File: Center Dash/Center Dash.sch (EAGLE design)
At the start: 90 parts, among them J1 502585-0470, Q1 BSS138, Q2 BSS138, Q3 BSS138, Q4 BSS138, U1 ADG3304BRUZ-REEL7, U2 TPS54540DDARQ1

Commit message: Fixed?? amp seal connector
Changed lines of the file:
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@@
 <?xml version="1.0" encoding="utf-8"?>
 <!DOCTYPE eagle SYSTEM "eagle.dtd">
-<eagle version="8.6.1">
+<eagle version="8.7.0">
 <drawing>
 <settings>
@@
 <part name="GND20" library="supply1" deviceset="GND" device=""/>
 <part name="GND21" library="supply1" deviceset="GND" device=""/>
-<part name="U$1" library="FormE" deviceset="TE-776200-1" device=""/>
 <part name="GND22" library="supply1" deviceset="GND" device=""/>
 <part name="P+7" library="supply1" deviceset="+15V" device=""/>
@@
 <part name="GND37" library="supply1" deviceset="GND" device=""/>
 <part name="+3V6" library="supply1" library_urn="urn:adsk.eagle:library:371" deviceset="+3V3" device=""/>
+<part name="U$1" library="FormE" deviceset="TE-776200-1" device=""/>
 </parts>
 <sheets>
@@
 <instance part="GND20" gate="1" x="317.5" y="-124.46"/>
 <instance part="GND21" gate="1" x="281.94" y="-124.46"/>
-<instance part="U$1" gate="G$1" x="403.86" y="-243.84"/>
 <instance part="GND22" gate="1" x="254" y="-304.8"/>
 <instance part="P+7" gate="1" x="457.2" y="-203.2"/>
@@
 <instance part="GND37" gate="1" x="340.36" y="-271.78"/>
 <instance part="+3V6" gate="G$1" x="203.2" y="-175.26"/>
+<instance part="U$1" gate="G$1" x="401.32" y="-243.84"/>
 </instances>
 <busses>
@@
 </segment>
 <segment>
-<pinref part="U$1" gate="G$1" pin="P19"/>
 <wire x1="416.56" y1="-264.16" x2="480.06" y2="-264.16" width="0.1524" layer="91"/>
 <label x="474.98" y="-264.16" size="1.778" layer="95"/>
-</segment>
-<segment>
-<pinref part="U$1" gate="G$1" pin="P16"/>
+<pinref part="U$1" gate="G$1" pin="P19"/>
+</segment>
+<segment>
 <wire x1="416.56" y1="-256.54" x2="457.2" y2="-256.54" width="0.1524" layer="91"/>
 <label x="452.12" y="-256.54" size="1.778" layer="95"/>
+<pinref part="U$1" gate="G$1" pin="P16"/>
 </segment>
 <segment>
@@
 </segment>
 <segment>
-<pinref part="U$1" gate="G$1" pin="P5"/>
 <wire x1="416.56" y1="-223.52" x2="426.72" y2="-223.52" width="0.1524" layer="91"/>
 <label x="421.64" y="-223.52" size="1.778" layer="95"/>
+<pinref part="U$1" gate="G$1" pin="P5"/>
 </segment>
 <segment>
@@
 </segment>
 <segment>
-<pinref part="U$1" gate="G$1" pin="P1"/>
 <wire x1="416.56" y1="-213.36" x2="457.2" y2="-213.36" width="0.1524" layer="91"/>
 <wire x1="457.2" y1="-213.36" x2="457.2" y2="-205.74" width="0.1524" layer="91"/>
 <pinref part="P+7" gate="1" pin="+15V"/>
+<pinref part="U$1" gate="G$1" pin="P1"/>
 </segment>
 <segment>
@@
 </segment>
 <segment>
-<pinref part="U$1" gate="G$1" pin="P18"/>
 <wire x1="416.56" y1="-261.62" x2="480.06" y2="-261.62" width="0.1524" layer="91"/>
 <label x="474.98" y="-261.62" size="1.778" layer="95"/>
-</segment>
-<segment>
-<pinref part="U$1" gate="G$1" pin="P2"/>
+<pinref part="U$1" gate="G$1" pin="P18"/>
+</segment>
+<segment>
 <wire x1="416.56" y1="-215.9" x2="426.72" y2="-215.9" width="0.1524" layer="91"/>
 <label x="421.64" y="-215.9" size="1.778" layer="95"/>
+<pinref part="U$1" gate="G$1" pin="P2"/>
 </segment>
 <segment>
@@
 <net name="SERVO_PWM" class="0">
 <segment>
-<pinref part="U$1" gate="G$1" pin="P3"/>
 <wire x1="416.56" y1="-218.44" x2="426.72" y2="-218.44" width="0.1524" layer="91"/>
 <label x="421.64" y="-218.44" size="1.778" layer="95"/>
+<pinref part="U$1" gate="G$1" pin="P3"/>
 </segment>
 <segment>
@@
 </segment>
 <segment>
-<pinref part="U$1" gate="G$1" pin="P11"/>
 <wire x1="416.56" y1="-241.3" x2="439.42" y2="-241.3" width="0.1524" layer="91"/>
 <label x="424.18" y="-241.3" size="1.778" layer="95"/>
 <wire x1="439.42" y1="-241.3" x2="439.42" y2="-210.82" width="0.1524" layer="91"/>
 <pinref part="R3" gate="G$1" pin="2"/>
+<pinref part="U$1" gate="G$1" pin="P11"/>
 </segment>
 </net>
@@
 </segment>
 <segment>
-<pinref part="U$1" gate="G$1" pin="P12"/>
 <label x="424.18" y="-243.84" size="1.778" layer="95"/>
 <wire x1="416.56" y1="-243.84" x2="444.5" y2="-243.84" width="0.1524" layer="91"/>
 <wire x1="444.5" y1="-243.84" x2="444.5" y2="-210.82" width="0.1524" layer="91"/>
 <pinref part="R5" gate="G$1" pin="2"/>
+<pinref part="U$1" gate="G$1" pin="P12"/>
 </segment>
 </net>
 <net name="SPARE_1" class="0">
 <segment>
-<pinref part="U$1" gate="G$1" pin="P8"/>
 <wire x1="416.56" y1="-231.14" x2="429.26" y2="-231.14" width="0.1524" layer="91"/>
 <label x="424.18" y="-231.14" size="1.778" layer="95"/>
+<pinref part="U$1" gate="G$1" pin="P8"/>
 </segment>
 <segment>
@@
 </segment>
 <segment>
-<pinref part="U$1" gate="G$1" pin="P4"/>
 <wire x1="416.56" y1="-220.98" x2="426.72" y2="-220.98" width="0.1524" layer="91"/>
 <label x="421.64" y="-220.98" size="1.778" layer="95"/>
+<pinref part="U$1" gate="G$1" pin="P4"/>
 </segment>
 </net>
@@
 </segment>
 <segment>
-<pinref part="U$1" gate="G$1" pin="P20"/>
 <wire x1="416.56" y1="-266.7" x2="480.06" y2="-266.7" width="0.1524" layer="91"/>
 <label x="469.9" y="-266.7" size="1.778" layer="95"/>
+<pinref part="U$1" gate="G$1" pin="P20"/>
 </segment>
 </net>
@@
 </segment>
 <segment>
-<pinref part="U$1" gate="G$1" pin="P21"/>
 <wire x1="416.56" y1="-269.24" x2="480.06" y2="-269.24" width="0.1524" layer="91"/>
 <label x="469.9" y="-269.24" size="1.778" layer="95"/>
+<pinref part="U$1" gate="G$1" pin="P21"/>
 </segment>
 </net>
@@
 </segment>
 <segment>
-<pinref part="U$1" gate="G$1" pin="P22"/>
 <wire x1="416.56" y1="-271.78" x2="480.06" y2="-271.78" width="0.1524" layer="91"/>
 <label x="469.9" y="-271.78" size="1.778" layer="95"/>
+<pinref part="U$1" gate="G$1" pin="P22"/>
 </segment>
 </net>
@@
 </segment>
 <segment>
-<pinref part="U$1" gate="G$1" pin="P23"/>
 <wire x1="416.56" y1="-274.32" x2="480.06" y2="-274.32" width="0.1524" layer="91"/>
 <label x="469.9" y="-274.32" size="1.778" layer="95"/>
+<pinref part="U$1" gate="G$1" pin="P23"/>
 </segment>
 </net>
@@
 </segment>
 <segment>
-<pinref part="U$1" gate="G$1" pin="P6"/>
 <label x="449.58" y="-226.06" size="1.778" layer="95"/>
 <wire x1="416.56" y1="-226.06" x2="457.2" y2="-226.06" width="0.1524" layer="91"/>
+<pinref part="U$1" gate="G$1" pin="P6"/>
 </segment>
 </net>
@@
 </segment>
 <segment>
-<pinref part="U$1" gate="G$1" pin="P7"/>
 <label x="449.58" y="-228.6" size="1.778" layer="95"/>
 <wire x1="416.56" y1="-228.6" x2="457.2" y2="-228.6" width="0.1524" layer="91"/>
+<pinref part="U$1" gate="G$1" pin="P7"/>
 </segment>
 </net>
@@
 </segment>
 <segment>
-<pinref part="U$1" gate="G$1" pin="P10"/>
 <wire x1="416.56" y1="-238.76" x2="457.2" y2="-238.76" width="0.1524" layer="91"/>
 <label x="449.58" y="-238.76" size="1.778" layer="95"/>
+<pinref part="U$1" gate="G$1" pin="P10"/>
 </segment>
 </net>
@@
 </segment>
 <segment>
-<pinref part="U$1" gate="G$1" pin="P9"/>
 <wire x1="416.56" y1="-236.22" x2="457.2" y2="-236.22" width="0.1524" layer="91"/>
 <label x="449.58" y="-236.22" size="1.778" layer="95"/>
+<pinref part="U$1" gate="G$1" pin="P9"/>
 </segment>
 </net>
@@
 </segment>
 <segment>
-<pinref part="U$1" gate="G$1" pin="P17"/>
 <wire x1="416.56" y1="-259.08" x2="480.06" y2="-259.08" width="0.1524" layer="91"/>
 <label x="469.9" y="-259.08" size="1.778" layer="95"/>
+<pinref part="U$1" gate="G$1" pin="P17"/>
 </segment>
 </net>
@@
 </segment>
 <segment>
-<pinref part="U$1" gate="G$1" pin="P13"/>
 <wire x1="416.56" y1="-246.38" x2="480.06" y2="-246.38" width="0.1524" layer="91"/>
 <label x="469.9" y="-246.38" size="1.778" layer="95"/>
+<pinref part="U$1" gate="G$1" pin="P13"/>
 </segment>
 </net>
@@
 </segment>
 <segment>
-<pinref part="U$1" gate="G$1" pin="P14"/>
 <wire x1="416.56" y1="-248.92" x2="480.06" y2="-248.92" width="0.1524" layer="91"/>
 <label x="469.9" y="-248.92" size="1.778" layer="95"/>
+<pinref part="U$1" gate="G$1" pin="P14"/>
 </segment>
 </net>
@@
 </segment>
 <segment>
-<pinref part="U$1" gate="G$1" pin="P15"/>
 <wire x1="416.56" y1="-251.46" x2="480.06" y2="-251.46" width="0.1524" layer="91"/>
 <label x="469.9" y="-251.46" size="1.778" layer="95"/>
-</segment>
-</net>
+<pinref part="U$1" gate="G$1" pin="P15"/>
+</segment>
+</net>

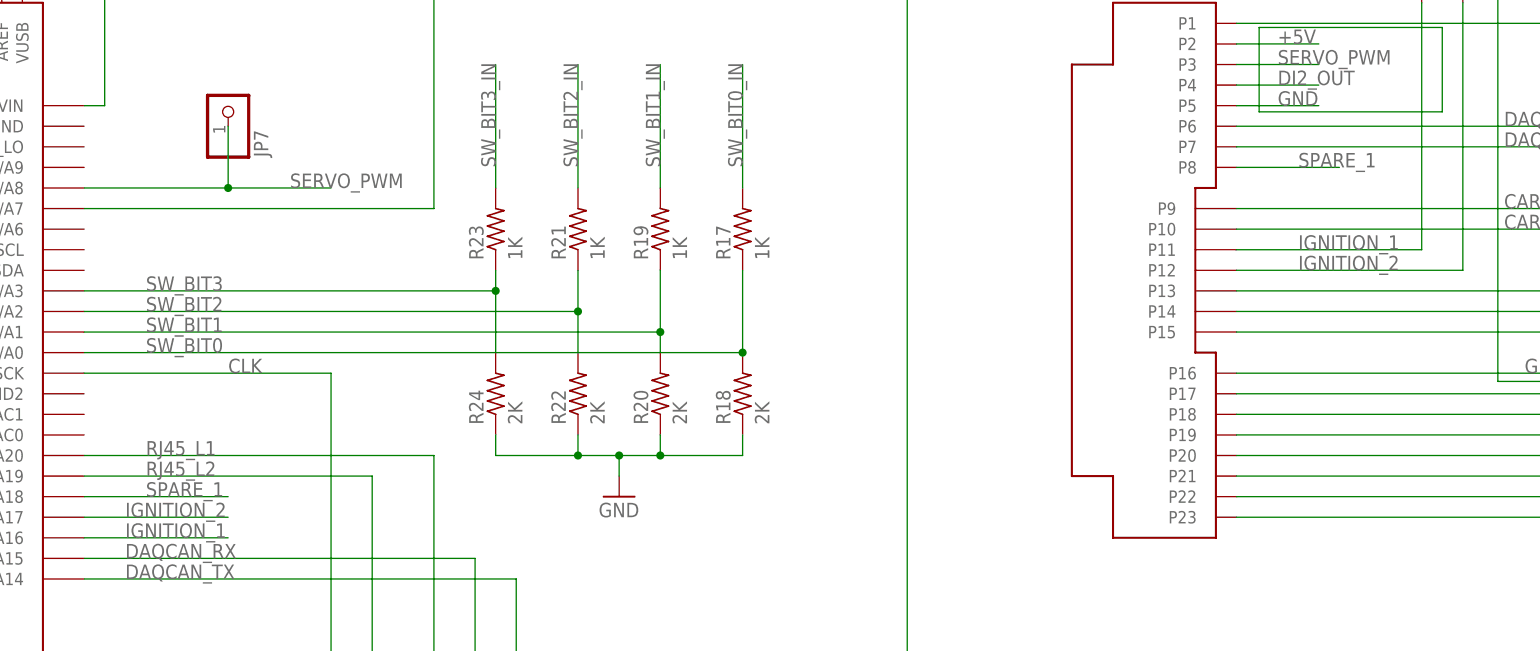
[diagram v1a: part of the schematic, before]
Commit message: Update schematic to remove last spare
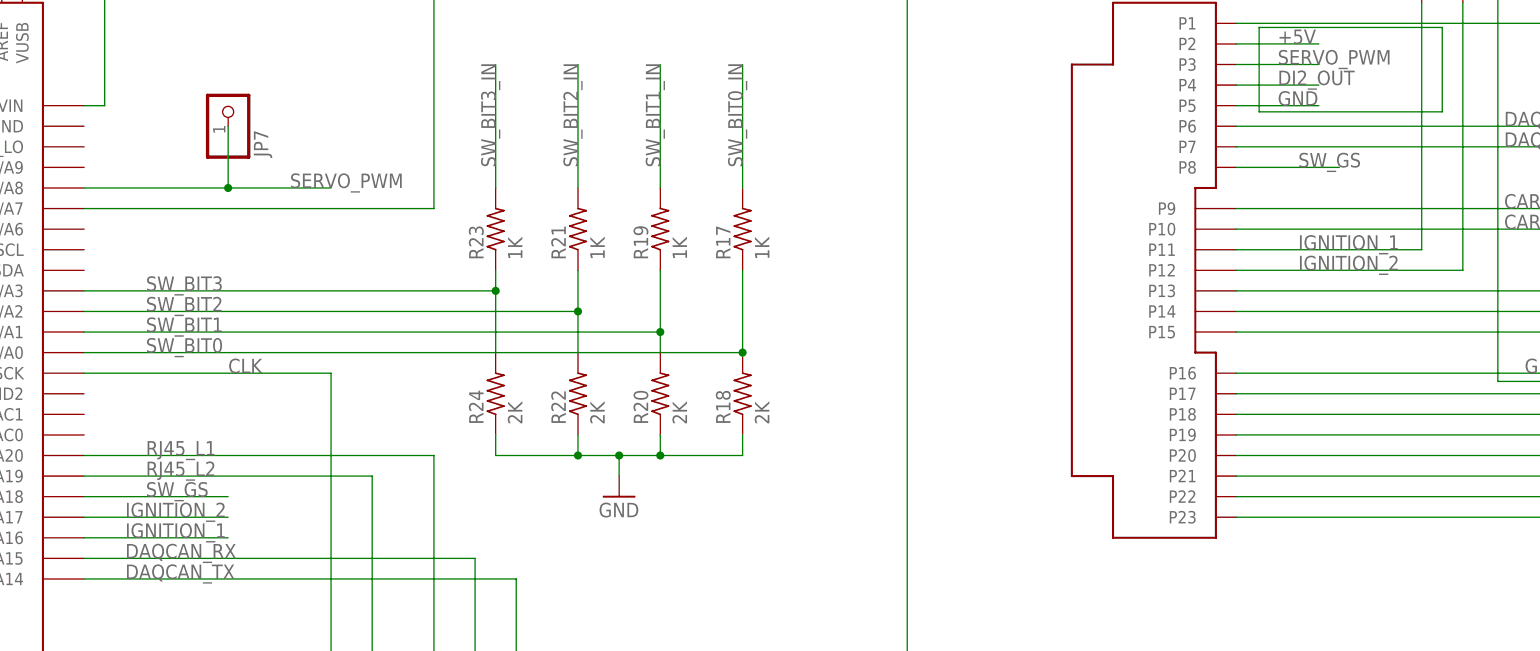
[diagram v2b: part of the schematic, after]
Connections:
- net SPARE_1 renamed SW_GS
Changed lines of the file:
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@@
-</segment>
-</net>
-<net name="SPARE_1" class="0">
-<segment>
-<wire x1="416.56" y1="-231.14" x2="429.26" y2="-231.14" width="0.1524" layer="91"/>
-<label x="424.18" y="-231.14" size="1.778" layer="95"/>
-<pinref part="U$1" gate="G$1" pin="P8"/>
-</segment>
-<segment>
-<pinref part="U$2" gate="G$1" pin="37/A18"/>
-<wire x1="274.32" y1="-271.78" x2="292.1" y2="-271.78" width="0.1524" layer="91"/>
-<label x="281.94" y="-271.78" size="1.778" layer="95"/>
 </segment>
 </net>
@@
 </segment>
 </net>
+<net name="SW_GS" class="0">
+<segment>
+<wire x1="416.56" y1="-231.14" x2="429.26" y2="-231.14" width="0.1524" layer="91"/>
+<label x="424.18" y="-231.14" size="1.778" layer="95"/>
+<pinref part="U$1" gate="G$1" pin="P8"/>
+</segment>
+<segment>
+<pinref part="U$2" gate="G$1" pin="37/A18"/>
+<wire x1="274.32" y1="-271.78" x2="292.1" y2="-271.78" width="0.1524" layer="91"/>
+<label x="281.94" y="-271.78" size="1.778" layer="95"/>
+</segment>
+</net>

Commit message: I dont remember
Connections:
- removed net N$1: LED2.GND
- net GND: now also LED2.GND
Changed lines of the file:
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@@
 <pinref part="LED6" gate="G$1" pin="GND"/>
 <wire x1="477.52" y1="-139.7" x2="477.52" y2="-144.78" width="0.1524" layer="91"/>
-<wire x1="477.52" y1="-144.78" x2="302.26" y2="-144.78" width="0.1524" layer="91"/>
+<wire x1="477.52" y1="-144.78" x2="444.5" y2="-144.78" width="0.1524" layer="91"/>
 <junction x="302.26" y="-144.78"/>
-</segment>
-<segment>
+<pinref part="LED2" gate="G$1" pin="GND"/>
+<wire x1="444.5" y1="-144.78" x2="408.94" y2="-144.78" width="0.1524" layer="91"/>
+<wire x1="408.94" y1="-144.78" x2="370.84" y2="-144.78" width="0.1524" layer="91"/>
+<wire x1="370.84" y1="-144.78" x2="335.28" y2="-144.78" width="0.1524" layer="91"/>
+<wire x1="335.28" y1="-144.78" x2="302.26" y2="-144.78" width="0.1524" layer="91"/>
+<wire x1="335.28" y1="-139.7" x2="335.28" y2="-144.78" width="0.1524" layer="91"/>
+<junction x="335.28" y="-144.78"/>
 <pinref part="LED3" gate="G$1" pin="GND"/>
 <wire x1="370.84" y1="-139.7" x2="370.84" y2="-144.78" width="0.1524" layer="91"/>
-</segment>
-<segment>
+<junction x="370.84" y="-144.78"/>
 <pinref part="LED4" gate="G$1" pin="GND"/>
 <wire x1="408.94" y1="-139.7" x2="408.94" y2="-144.78" width="0.1524" layer="91"/>
-</segment>
-<segment>
+<junction x="408.94" y="-144.78"/>
 <pinref part="LED5" gate="G$1" pin="GND"/>
 <wire x1="444.5" y1="-139.7" x2="444.5" y2="-144.78" width="0.1524" layer="91"/>
-</segment>
-<segment>
-<pinref part="LED8" gate="G$1" pin="GND"/>
-<wire x1="447.04" y1="-96.52" x2="447.04" y2="-101.6" width="0.1524" layer="91"/>
-</segment>
-<segment>
-<pinref part="LED9" gate="G$1" pin="GND"/>
-<wire x1="411.48" y1="-96.52" x2="411.48" y2="-101.6" width="0.1524" layer="91"/>
-</segment>
-<segment>
-<pinref part="LED10" gate="G$1" pin="GND"/>
-<wire x1="375.92" y1="-96.52" x2="375.92" y2="-101.6" width="0.1524" layer="91"/>
-</segment>
-<segment>
-<pinref part="LED11" gate="G$1" pin="GND"/>
-<wire x1="340.36" y1="-96.52" x2="340.36" y2="-101.6" width="0.1524" layer="91"/>
+<junction x="444.5" y="-144.78"/>
 </segment>
 <segment>
@@
 <pinref part="LED7" gate="G$1" pin="GND"/>
 <wire x1="480.06" y1="-96.52" x2="480.06" y2="-101.6" width="0.1524" layer="91"/>
-<wire x1="480.06" y1="-101.6" x2="304.8" y2="-101.6" width="0.1524" layer="91"/>
+<wire x1="480.06" y1="-101.6" x2="447.04" y2="-101.6" width="0.1524" layer="91"/>
 <junction x="304.8" y="-101.6"/>
+<pinref part="LED8" gate="G$1" pin="GND"/>
+<wire x1="447.04" y1="-101.6" x2="411.48" y2="-101.6" width="0.1524" layer="91"/>
+<wire x1="411.48" y1="-101.6" x2="375.92" y2="-101.6" width="0.1524" layer="91"/>
+<wire x1="375.92" y1="-101.6" x2="340.36" y2="-101.6" width="0.1524" layer="91"/>
+<wire x1="340.36" y1="-101.6" x2="304.8" y2="-101.6" width="0.1524" layer="91"/>
+<wire x1="447.04" y1="-96.52" x2="447.04" y2="-101.6" width="0.1524" layer="91"/>
+<junction x="447.04" y="-101.6"/>
+<pinref part="LED9" gate="G$1" pin="GND"/>
+<wire x1="411.48" y1="-96.52" x2="411.48" y2="-101.6" width="0.1524" layer="91"/>
+<junction x="411.48" y="-101.6"/>
+<pinref part="LED10" gate="G$1" pin="GND"/>
+<wire x1="375.92" y1="-96.52" x2="375.92" y2="-101.6" width="0.1524" layer="91"/>
+<junction x="375.92" y="-101.6"/>
+<pinref part="LED11" gate="G$1" pin="GND"/>
+<wire x1="340.36" y1="-96.52" x2="340.36" y2="-101.6" width="0.1524" layer="91"/>
+<junction x="340.36" y="-101.6"/>
 </segment>
 <segment>
@@
 </segment>
 </net>
-<net name="N$1" class="0">
-<segment>
-<pinref part="LED2" gate="G$1" pin="GND"/>
-<wire x1="335.28" y1="-139.7" x2="335.28" y2="-144.78" width="0.1524" layer="91"/>
-</segment>
-</net>

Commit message: Fixed Ignition 2
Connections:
- net IGNITION_2: now also U$2.20/A6
